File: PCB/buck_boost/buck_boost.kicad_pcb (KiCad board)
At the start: 4 copper layers, 80 x 70 mm, 60 parts, among them J1 VIN 10-24V, J2 VOUT, J3 VOUT, J4 VOUT, J5 VOUT, Q1 TK1R4S04PB, Q2 TK1R4S04PB, Q3 TK1R4S04PB, Q4 TK1R4S04PB, Q5 TK1R4S04PB, U1 LTC4359-MS8, U2 LT8392

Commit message: Update buck_boost to kicad 6
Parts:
- D2, D3: value SMD24PL-TP -> SS2040LL
- L1: value 15µF -> 15µH
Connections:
- net /~PGOOD renamed /~{PGOOD}
- RV2 pad 3: Net-(RV2-Pad3) -> unconnected-(RV2-Pad3)
- U1 pad 3: Net-(U1-Pad3) -> unconnected-(U1-Pad3)
- U1 pad 7: Net-(U1-Pad7) -> unconnected-(U1-Pad7)
- U2 pad 16: Net-(U2-Pad16) -> unconnected-(U2-Pad16)
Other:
- net class Default removed

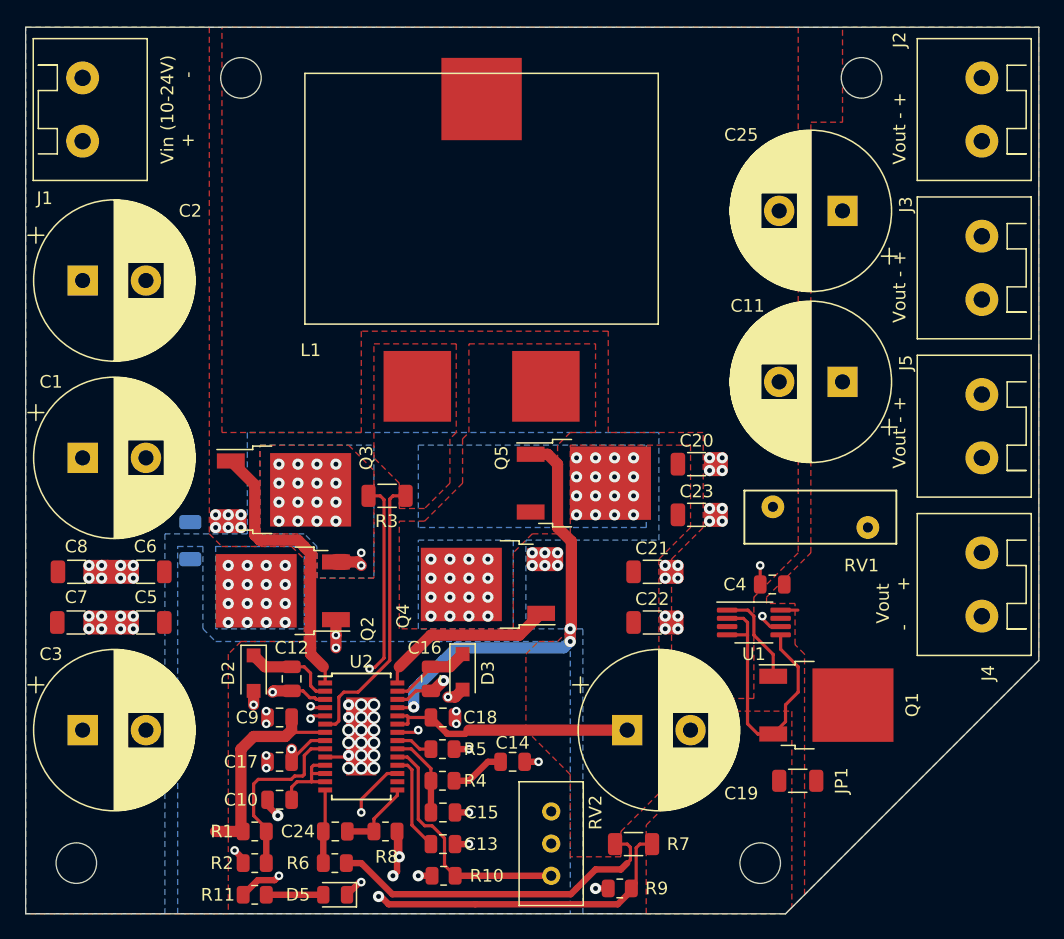
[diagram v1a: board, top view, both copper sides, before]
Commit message: Add a PI filter to buck_boost. Fix ringing for other PI filters.
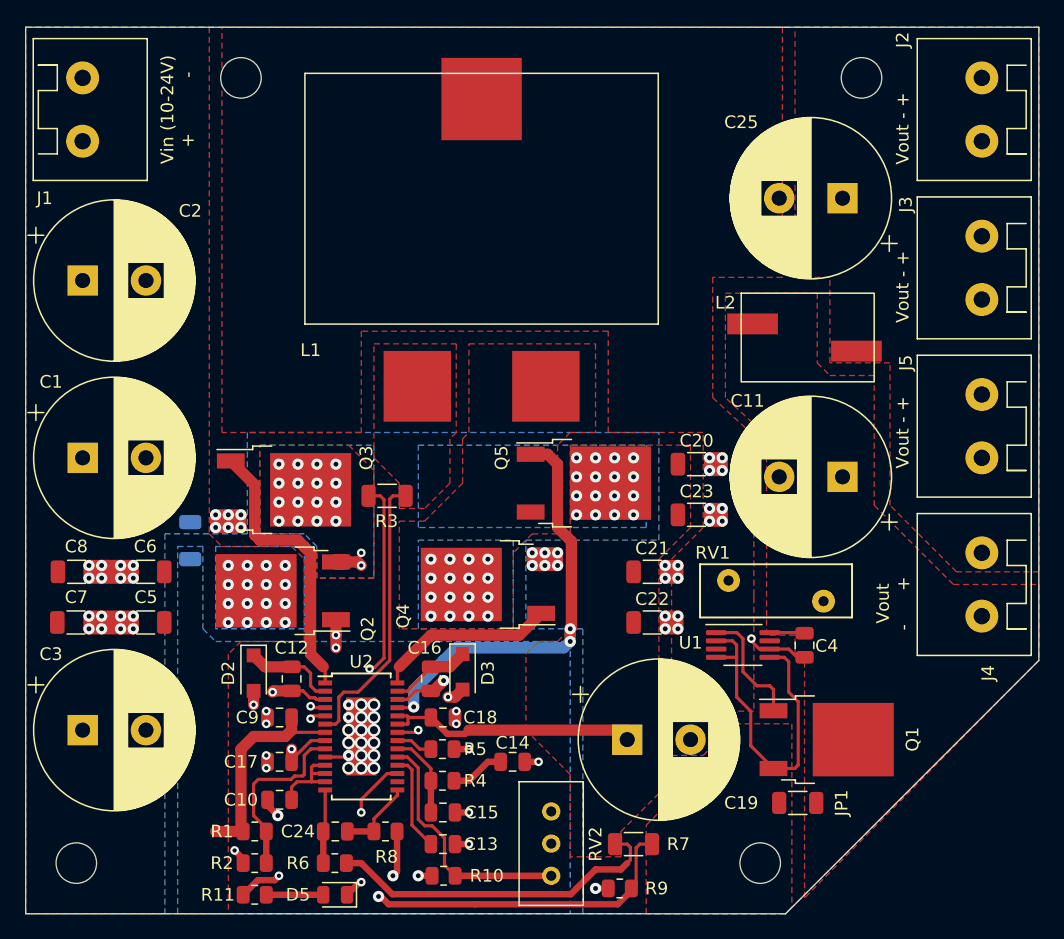
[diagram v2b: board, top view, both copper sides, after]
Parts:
- added L2: 1µH (PA4987.102HLT), t-top:PA4987.XXXHL, F.Cu at (86.5, 44.5)
- L1: value 15µH -> 15µH (PQ2617BHA-150K)
- moved C11 7.50 mm to (89.5, 55.5)
- moved RV1 6.79 mm to (88.0, 65.3)
- moved C4 5.44 mm to (86.5, 68.8), turned to -90 degrees
- moved Q1 2.73 mm to (88.2, 76.2)
- moved U1 1.97 mm to (81.6, 68.8)
- moved JP1 1.75 mm to (86.0, 81.2)
- moved C25 1.00 mm to (89.5, 33.5)
- moved C19 0.75 mm to (72.5, 76.2)
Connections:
- C25 pad 1: Net-(C11-Pad1) -> Net-(C25-Pad1)
- J2 pad 2: Net-(C11-Pad1) -> Net-(C25-Pad1)
- J3 pad 2: Net-(C11-Pad1) -> Net-(C25-Pad1)
- J4 pad 2: Net-(C11-Pad1) -> Net-(C25-Pad1)
- J5 pad 2: Net-(C11-Pad1) -> Net-(C25-Pad1)
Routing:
- net Net-(Q1-Pad1): track 7.69 -> 9.59 mm
- net GNDPWR: track 59.7 -> 61.3 mm, vias 52 -> 51
- net /REG_OUT: track 56.3 -> 57.8 mm, vias 3 -> 2
- net Net-(C11-Pad1): track 1.36 -> 2.77 mm
- net +5V: track 47.5 -> 46.1 mm
- net Net-(C18-Pad1): track 47.6 -> 48.8 mm
- added copper zone on F.Cu, net Net-(C25-Pad1)
